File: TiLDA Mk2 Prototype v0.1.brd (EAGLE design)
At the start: 67.9 x 100 mm, 199 parts, among them IC1 ATSAM3X8EA-AU, IC10 MCP73831, IC2 MPU-6050, IC3 SRF-V1.2, IC5 S25FL216K0PMFI011, IC7 HMC5883LSMD (NP), IC8 MCP1825T-3302E/DC, IC9 TC1015-3V3, J1 ZX62-AB-5PA(11), J3 Arduino Headers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

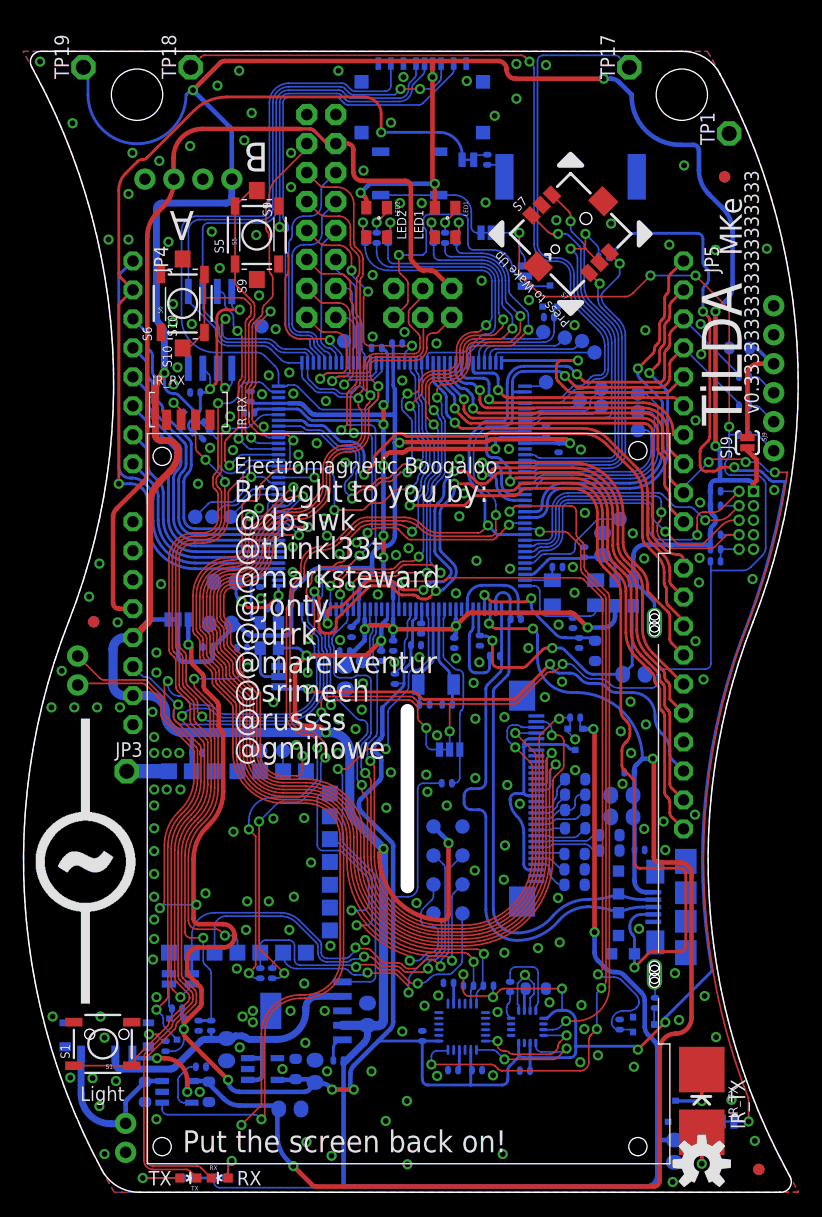
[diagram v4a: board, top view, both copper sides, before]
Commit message: Prototype : Flipped IR_RX around for easier hand soldering
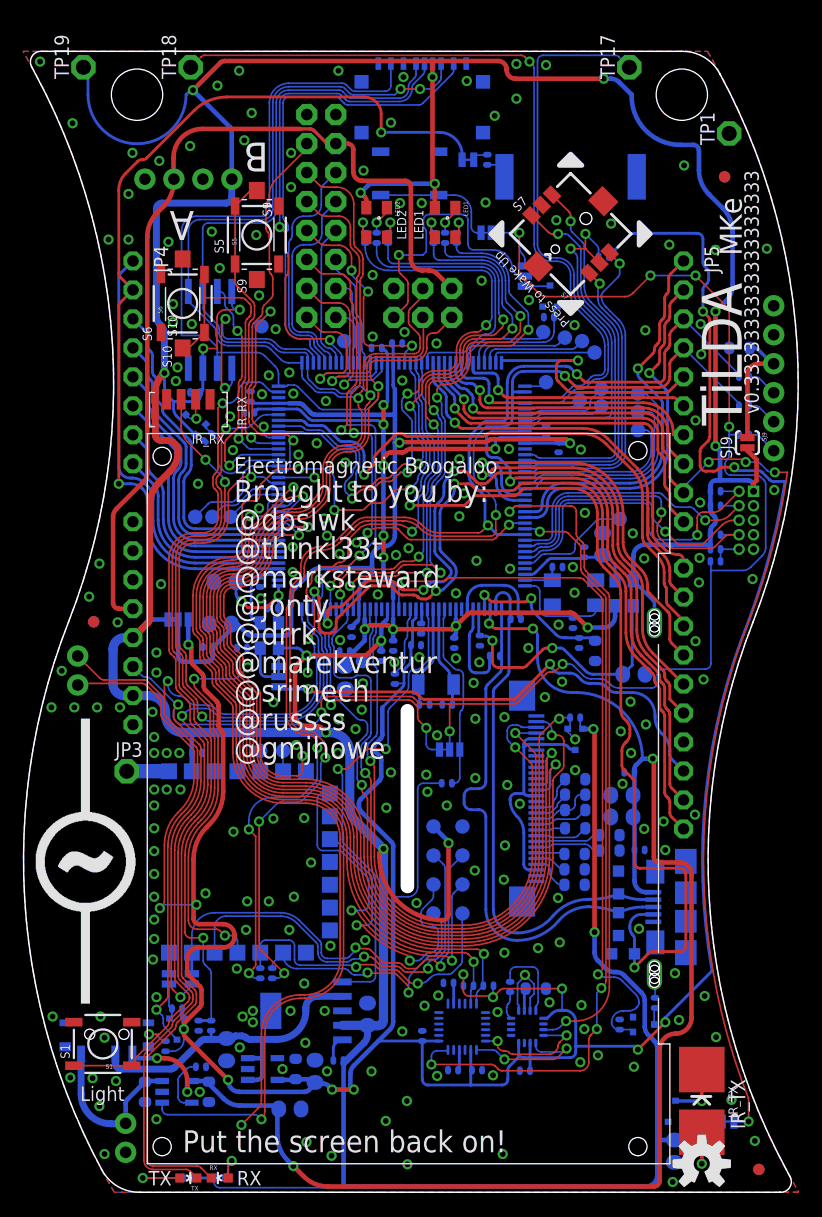
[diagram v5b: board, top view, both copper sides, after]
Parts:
- moved Q13 0.28 mm to (14.9, 67.5)
- moved R49 0.28 mm to (16.3, 66.2)
- turned IR_RX to 180 degrees
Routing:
- net IR_RX: track 49.2 -> 51.5 mm
- net 3V3: track 521.0 -> 519.7 mm
- net MISO: track 159.5 -> 160.6 mm
- net GND: vias 234 -> 233

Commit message: Prototype: Tweaks
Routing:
- net GND: vias 233 -> 235
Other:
- board text added: "@CharlesYarnold"
- board text added: "C109"
- board text added: "Q11"
- board text removed: "R109"
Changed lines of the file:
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@@
 <text x="46.6" y="50.6" size="0.6096" layer="22" font="vector" ratio="15" rot="MR270">C122</text>
 <text x="44.3" y="48.9" size="0.6096" layer="22" font="vector" ratio="15" rot="MR0">R105</text>
-<text x="39" y="47.3" size="0.6096" layer="22" font="vector" ratio="15" rot="MR90">R109</text>
+<text x="39" y="47.3" size="0.6096" layer="22" font="vector" ratio="15" rot="MR90">C109</text>
 <text x="42.5" y="45.9" size="0.6096" layer="22" font="vector" ratio="15" rot="MR0">R106</text>
 <text x="36.6" y="47.1" size="0.6096" layer="22" font="vector" ratio="15" rot="MR90">C114</text>
@@
 <text x="51.6" y="39.2" size="0.6096" layer="22" font="vector" ratio="15" rot="MR0">C39</text>
 <text x="49.2" y="43.1" size="0.6096" layer="22" font="vector" ratio="15" rot="MR0">R44</text>
-<text x="49.2" y="42.3" size="0.6096" layer="22" font="vector" ratio="15" rot="MR0">Q10</text>
+<text x="49.2" y="42.3" size="0.6096" layer="22" font="vector" ratio="15" rot="MR0">Q11</text>
 <text x="45.8" y="26.1" size="0.6096" layer="22" font="vector" ratio="15" rot="MR270">J7</text>
 <text x="52.9" y="60" size="0.8128" layer="22" font="vector" ratio="15" rot="MR0">26</text>
@@
 <text x="14.2" y="52.55" size="0.8128" layer="22" font="vector" ratio="15" rot="MR90">VBACKUP</text>
 <text x="12.2" y="52.55" size="0.8128" layer="22" font="vector" ratio="15" rot="MR90">3V3</text>
-<text x="15.3" y="4" size="0.8128" layer="22" font="vector" ratio="15" rot="MR180">BLACK</text>
-<text x="15.5" y="6.3" size="0.8128" layer="22" font="vector" ratio="15" rot="MR180">RED</text>
+<text x="15.3" y="4" size="1.016" layer="22" font="vector" ratio="15" rot="MR180">BLACK</text>
+<text x="15.5" y="6.3" size="1.016" layer="22" font="vector" ratio="15" rot="MR180">RED</text>
 <text x="55.5" y="1" size="1.9304" layer="22" font="vector" ratio="20" rot="MR0">badge.emfcamp.org/2014</text>
 <text x="63" y="82.1" size="1.9304" layer="21" font="vector" ratio="15" rot="R90">MKe</text>
@@
 <text x="18.5" y="58" size="1.9304" layer="21" font="vector" ratio="15">@dpslwk</text>
 <text x="18.5" y="55.5" size="1.9304" layer="21" font="vector" ratio="15">@thinkl33t</text>
-<text x="18.5" y="50.5" size="1.9304" layer="21" font="vector" ratio="15">@jonty</text>
-<text x="18.5" y="53" size="1.9304" layer="21" font="vector" ratio="15">@marksteward</text>
-<text x="18.5" y="48" size="1.9304" layer="21" font="vector" ratio="15">@drrk</text>
-<text x="18.5" y="43" size="1.9304" layer="21" font="vector" ratio="15">@srimech</text>
-<text x="18.5" y="45.5" size="1.9304" layer="21" font="vector" ratio="15">@marekventur</text>
-<text x="18.5" y="40.5" size="1.9304" layer="21" font="vector" ratio="15">@russss</text>
+<text x="18.5" y="48" size="1.9304" layer="21" font="vector" ratio="15">@jonty</text>
+<text x="18.5" y="50.5" size="1.9304" layer="21" font="vector" ratio="15">@CharlesYarnold</text>
+<text x="18.5" y="45.5" size="1.9304" layer="21" font="vector" ratio="15">@drrk</text>
+<text x="18.5" y="40.5" size="1.9304" layer="21" font="vector" ratio="15">@srimech</text>
+<text x="18.5" y="43" size="1.9304" layer="21" font="vector" ratio="15">@marekventur</text>
+<text x="18.5" y="38" size="1.9304" layer="21" font="vector" ratio="15">@russss</text>
 <text x="14" y="3.5" size="1.9304" layer="21" font="vector" ratio="20">Put the screen back on!</text>
 <text x="41.5" y="52.5" size="0.8128" layer="22" font="vector" ratio="15" rot="MR45">You did not see this. Tell no one.</text>
-<text x="18.5" y="38" size="1.9304" layer="21" font="vector" ratio="15">@gmjhowe</text>
+<text x="18.5" y="35.5" size="1.9304" layer="21" font="vector" ratio="15">@gmjhowe</text>
 <text x="5.5" y="16.8" size="0.8128" layer="22" font="vector" ratio="15" rot="MR90">On/Battery</text>
+<text x="18.5" y="53" size="1.9304" layer="21" font="vector" ratio="15">@marksteward</text>
 </plain>
 <attributes>
@@
 <contactref element="S10" pad="2"/>
 <via x="18.4" y="65.05" extent="1-16" drill="0.5"/>
-<wire x1="5" y1="65.05" x2="5" y2="65.05" width="0" layer="19" extent="1-16"/>
 <via x="12.1" y="53.3" extent="1-16" drill="0.5"/>
 <via x="31.85" y="33.7" extent="1-16" drill="0.5"/>
@@
 <via x="50.4" y="12" extent="1-16" drill="0.5"/>
 <via x="48.85" y="11.4" extent="1-16" drill="0.5"/>
-<wire x1="12.595" y1="69.5" x2="5" y2="65.05" width="0" layer="19" extent="1-1"/>
-<wire x1="15.4" y1="14.1555" x2="16.0445" y2="11" width="0" layer="19" extent="16-16"/>
+<via x="18.75" y="19.6" extent="1-16" drill="0.5"/>
+<via x="16.15" y="18.7" extent="1-16" drill="0.5"/>
 </signal>
 <signal name="LCD_CS">
@@
 <contactref element="IC3" pad="17"/>
 <wire x1="26.9" y1="30.95" x2="27.3" y2="30.95" width="0.15" layer="16"/>
-<wire x1="27.3" y1="30.95" x2="30.453553125" y2="27.796446875" width="0.15" layer="16"/>
-<wire x1="30.453553125" y1="27.796446875" x2="30.6" y2="27.44289375" width="0.15" layer="16" curve="-45"/>
-<wire x1="30.6" y1="27.44289375" x2="30.6" y2="23.9" width="0.15" layer="16"/>
+<wire x1="27.3" y1="30.95" x2="29.721321875" y2="28.528678125" width="0.15" layer="16"/>
+<wire x1="29.721321875" y1="28.528678125" x2="30.6" y2="26.407359375" width="0.15" layer="16" curve="-44.99994"/>
+<wire x1="30.6" y1="26.407359375" x2="30.6" y2="23.9" width="0.15" layer="16"/>
 <wire x1="30.6" y1="23.9" x2="30.1" y2="23.4" width="0.15" layer="16" curve="-90"/>
 <wire x1="30.1" y1="23.4" x2="29.25" y2="23.4" width="0.15" layer="16"/>
@@
 <wire x1="26.3" y1="29.95" x2="27.64289375" y2="29.95" width="0.15" layer="16"/>
 <wire x1="27.64289375" y1="29.95" x2="27.996446875" y2="29.803553125" width="0.15" layer="16" curve="-45"/>
-<wire x1="27.996446875" y1="29.803553125" x2="30.153553125" y2="27.646446875" width="0.15" layer="16"/>
-<wire x1="30.153553125" y1="27.646446875" x2="30.3" y2="27.29289375" width="0.15" layer="16" curve="-45"/>
-<wire x1="30.3" y1="27.29289375" x2="30.3" y2="25.2" width="0.15" layer="16"/>
+<wire x1="27.996446875" y1="29.803553125" x2="29.421321875" y2="28.378678125" width="0.15" layer="16"/>
+<wire x1="29.421321875" y1="28.378678125" x2="30.3" y2="26.257359375" width="0.15" layer="16" curve="-44.99994"/>
+<wire x1="30.3" y1="26.257359375" x2="30.3" y2="25.2" width="0.15" layer="16"/>
 <wire x1="30.3" y1="25.2" x2="29.8" y2="24.7" width="0.15" layer="16" curve="-90"/>
 <wire x1="29.8" y1="24.7" x2="28.8" y2="24.7" width="0.15" layer="16"/>
@@
 <wire x1="28" y1="36.49289375" x2="28" y2="30.90710625" width="0.15" layer="16"/>
 <wire x1="28" y1="30.90710625" x2="28.146446875" y2="30.553553125" width="0.15" layer="16" curve="45"/>
-<wire x1="28.146446875" y1="30.553553125" x2="30.753553125" y2="27.946446875" width="0.15" layer="16"/>
-<wire x1="30.753553125" y1="27.946446875" x2="30.9" y2="27.59289375" width="0.15" layer="16" curve="-45"/>
-<wire x1="30.9" y1="27.59289375" x2="30.9" y2="18.95" width="0.15" layer="16"/>
+<wire x1="28.146446875" y1="30.553553125" x2="30.021321875" y2="28.678678125" width="0.15" layer="16"/>
+<wire x1="30.021321875" y1="28.678678125" x2="30.9" y2="26.557359375" width="0.15" layer="16" curve="-44.99994"/>
+<wire x1="30.9" y1="26.557359375" x2="30.9" y2="18.95" width="0.15" layer="16"/>
 <wire x1="30.9" y1="18.95" x2="30.4" y2="18.45" width="0.15" layer="16" curve="-90"/>
 <wire x1="30.4" y1="18.45" x2="28" y2="18.45" width="0.15" layer="16"/>
@@
 <via x="14.4" y="8.8" extent="1-16" drill="0.5"/>
 <wire x1="14.4" y1="8.8" x2="14.4" y2="9.75" width="0.4064" layer="16"/>
-<wire x1="14.4" y1="9.75" x2="14.8" y2="9.75" width="0.4064" layer="16"/>
-<wire x1="14.8" y1="9.75" x2="14.8001" y2="9.75" width="0" layer="19" extent="16-16"/>
+<wire x1="14.4" y1="9.75" x2="14.8001" y2="9.75" width="0.4064" layer="16"/>
+<wire x1="14.8001" y1="9.75" x2="14.8" y2="9.7499" width="0.4064" layer="16" curve="90"/>
+<wire x1="14.8" y1="9.7499" x2="14.8" y2="9.7" width="0.4064" layer="16"/>
 </signal>
 <signal name="JTAG_RESET">
@@
 <contactref element="R38" pad="1"/>
 <wire x1="16.5" y1="15.0445" x2="15.4" y2="15.0445" width="0.254" layer="16"/>
-<wire x1="16.5" y1="15.0445" x2="16.5" y2="19.19289375" width="0.15" layer="16"/>
-<wire x1="16.5" y1="19.19289375" x2="16.353553125" y2="19.546446875" width="0.15" layer="16" curve="45"/>
-<wire x1="16.353553125" y1="19.546446875" x2="15.946446875" y2="19.953553125" width="0.15" layer="16"/>
-<wire x1="15.946446875" y1="19.953553125" x2="15.8" y2="20.30710625" width="0.15" layer="16" curve="-45"/>
-<wire x1="15.8" y1="20.30710625" x2="15.8" y2="22.3" width="0.15" layer="16"/>
+<wire x1="16.5" y1="15.0445" x2="16.5" y2="15.1" width="0.15" layer="16"/>
+<wire x1="16.5" y1="15.1" x2="16.60710625" y2="15.20710625" width="0.15" layer="16"/>
+<wire x1="16.60710625" y1="15.20710625" x2="16.9" y2="15.9142125" width="0.15" layer="16" curve="45"/>
+<wire x1="16.9" y1="15.9142125" x2="16.9" y2="18.5857875" width="0.15" layer="16"/>
+<wire x1="16.9" y1="18.5857875" x2="16.60710625" y2="19.29289375" width="0.15" layer="16" curve="45"/>
+<wire x1="16.60710625" y1="19.29289375" x2="15.8" y2="20.1" width="0.15" layer="16"/>
+<wire x1="15.8" y1="20.1" x2="15.8" y2="22.3" width="0.15" layer="16"/>
 <via x="15.8" y="22.3" extent="1-16" drill="0.5"/>
 <wire x1="15.8" y1="22.3" x2="14.7" y2="22.3" width="0.15" layer="1"/>
